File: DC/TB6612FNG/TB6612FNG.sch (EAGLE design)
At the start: 13 parts

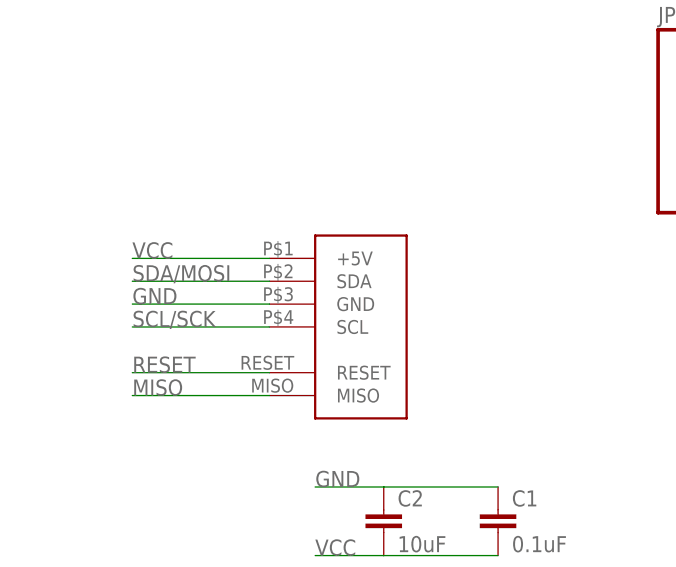
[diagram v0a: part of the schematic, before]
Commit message: Mostly re-routed the TB6612FNG based motor driver board for the v2 footprint. Not finished, since I'm planning to abandon this chip.
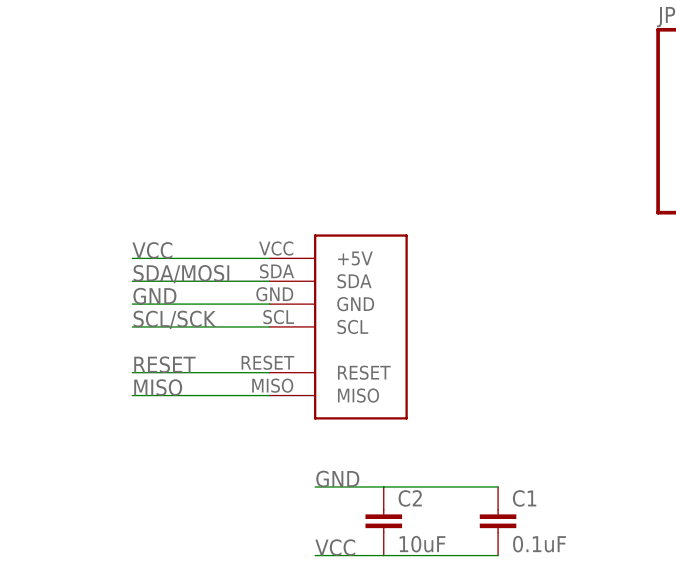
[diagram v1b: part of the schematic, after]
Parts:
- U$4: value FOOTPRINT -> FOOTPRINTFOOTPRINT-2; device IntegerLabs:FOOTPRINT -> IntegerLabs:FOOTPRINTFOOTPRINT-2
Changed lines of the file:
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@@
 <part name="LED" library="led" deviceset="LED" device="CHIPLED_1206" value="blue"/>
 <part name="U$3" library="IntegerLabs" deviceset="TINY841" device=""/>
-<part name="U$4" library="IntegerLabs" deviceset="FOOTPRINT" device=""/>
+<part name="U$4" library="IntegerLabs" deviceset="FOOTPRINT" device="FOOTPRINT-2" value="FOOTPRINTFOOTPRINT-2"/>
 <part name="U$1" library="IntegerLabs" deviceset="TB6612FNG" device=""/>
 <part name="JP2" library="SparkFun-Connectors" deviceset="M07" device=""/>
